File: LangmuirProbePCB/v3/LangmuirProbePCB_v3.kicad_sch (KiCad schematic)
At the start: 12 parts, among them U1 LM741, U2 OPA454AIDDA

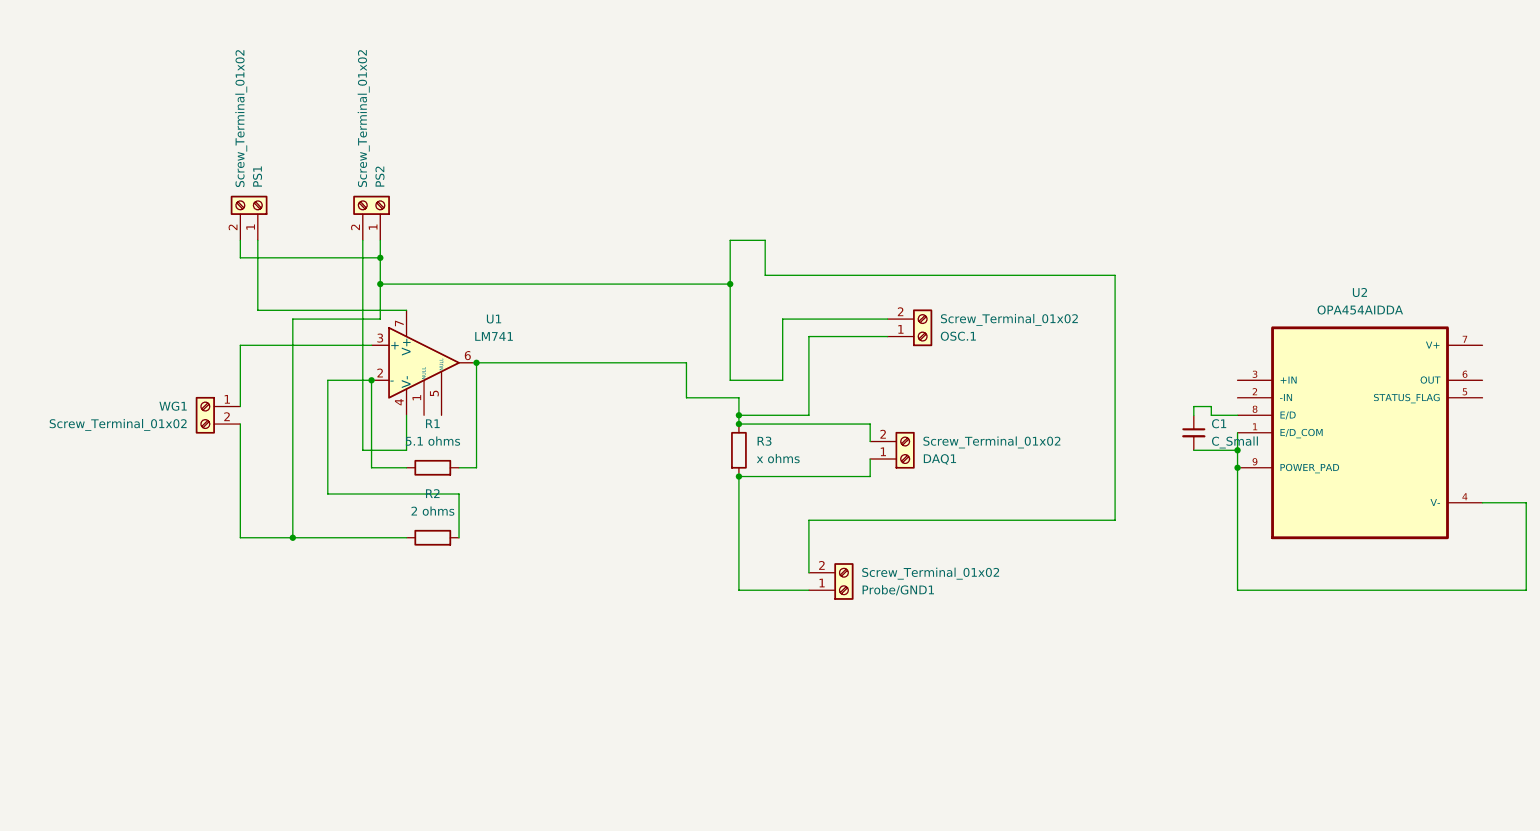
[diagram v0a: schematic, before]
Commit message: added v3 with OPA454
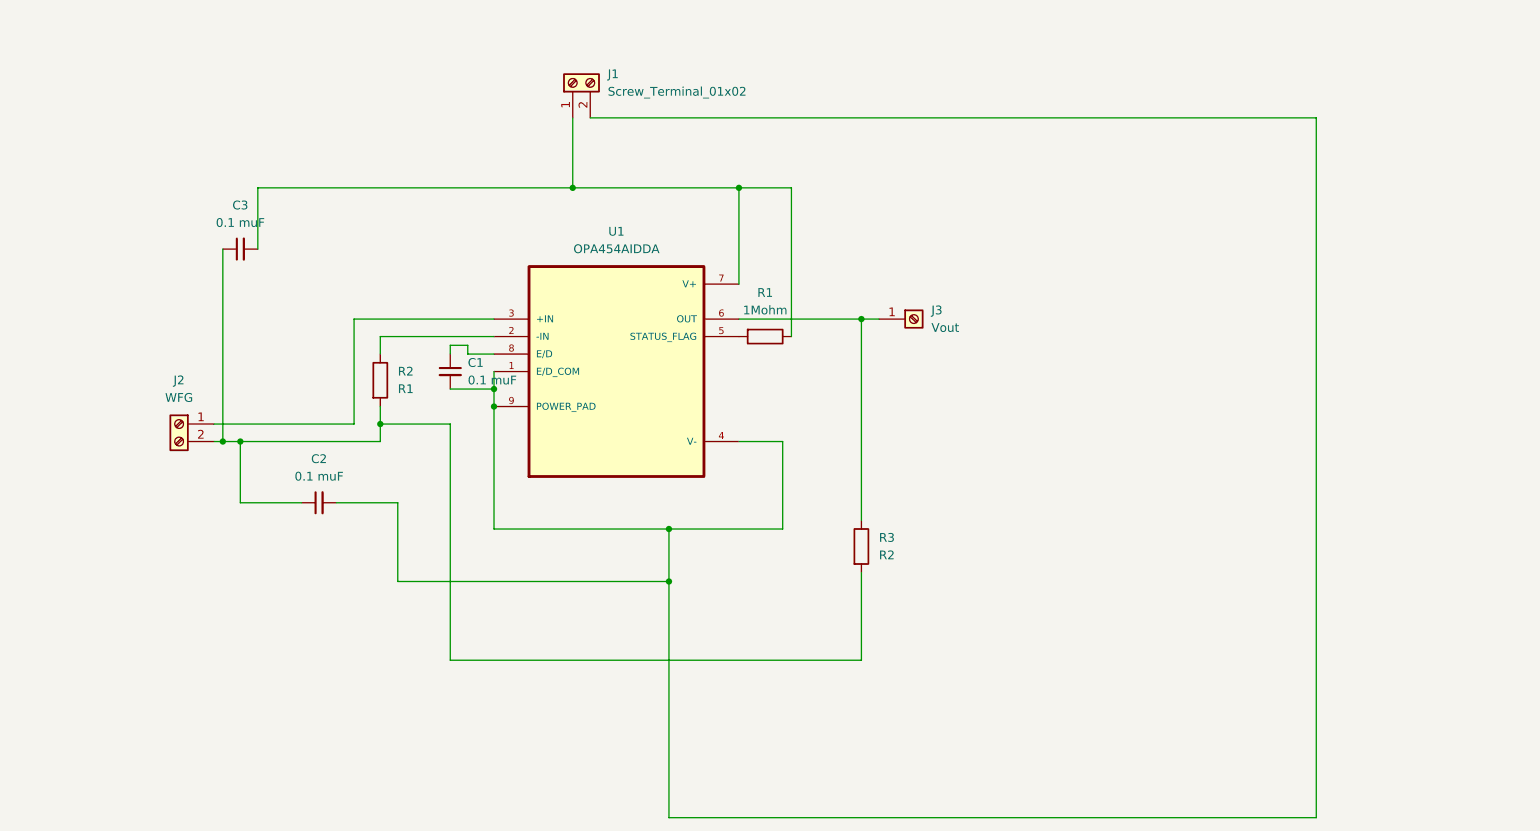
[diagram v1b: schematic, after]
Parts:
- removed DAQ1, OSC.1, PS1, PS2, Probe/GND1, WG1: Screw_Terminal_01x02, TerminalBlock_Phoenix:TerminalBlock_Phoenix_MPT-0,5-2-2.54_1x02_P2.54mm_Horizontal, symbol Connector:Screw_Terminal_01x02
- removed U1: LM741, LM741CN_NOPB:DIP794W45P254L959H508Q8, symbol Amplifier_Operational:LM741
- removed U2: OPA454AIDDA, OPA454AIDDA:VREG_LM5017MR_NOPB, symbol OPA454AIDDA:OPA454AIDDA
- added C2, C3: 0.1 muF, Capacitor_SMD:C_0201_0603Metric, symbol Device:C_Small
- added J1: Screw_Terminal_01x02, TerminalBlock_Phoenix:TerminalBlock_Phoenix_MPT-0,5-2-2.54_1x02_P2.54mm_Horizontal, symbol Connector:Screw_Terminal_01x02
- added J2: WFG, TerminalBlock_Phoenix:TerminalBlock_Phoenix_MPT-0,5-2-2.54_1x02_P2.54mm_Horizontal, symbol Connector:Screw_Terminal_01x02
- added J3: Vout, Connector_TE-Connectivity:TE_MATE-N-LOK_1-794374-x_1x01_P4.14mm_Horizontal, symbol Connector:Screw_Terminal_01x01
- added U1: OPA454AIDDA, OPA454AIDDA:VREG_LM5017MR_NOPB, symbol OPA454AIDDA:OPA454AIDDA
- C1: value C_Small -> 0.1 muF
- R1: value 5.1 ohms -> 1Mohm; footprint Resistor_THT:R_Axial_DIN0207_L6.3mm_D2.5mm_P7.62mm_Horizontal -> Resistor_THT:R_Axial_DIN0204_L3.6mm_D1.6mm_P7.62mm_Horizontal
- R2: value 2 ohms -> R1; footprint Resistor_THT:R_Axial_DIN0207_L6.3mm_D2.5mm_P7.62mm_Horizontal -> Resistor_THT:R_Axial_DIN0204_L3.6mm_D1.6mm_P7.62mm_Horizontal
- R3: value x ohms -> R2; footprint Resistor_THT:R_Axial_DIN0207_L6.3mm_D2.5mm_P7.62mm_Horizontal -> Resistor_THT:R_Axial_DIN0204_L3.6mm_D1.6mm_P7.62mm_Horizontal
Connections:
- net at R3.1: now also J3.1 (Pin_1), U1.6 (OUT); no longer R1.2
- net at R3.2: now also R2.2, C2.1, C3.1, J2.2 (Pin_2)
- net at R2.1: now also U1.2 (-IN)
- net at C1.2: now also C2.2, J1.2 (Pin_2), U1.1 (E/D_COM), U1.4 (V-), U1.9 (POWER_PAD)
- net at C1.1: now also U1.8 (E/D)
- net at R1.1: now also C3.2, J1.1 (Pin_1), U1.7 (V+); no longer R2.2
- new net: J2.1 (Pin_1), U1.3 (+IN)
- new net: R1.2, U1.5 (STATUS_FLAG)
